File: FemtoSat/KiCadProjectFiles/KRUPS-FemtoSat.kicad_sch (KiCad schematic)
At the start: 51 parts, among them J1 XT30U Male Connector, J2 54-00170, J3 USB_C_Receptacle_USB2.0_16P, Q1 IRF7410, Q2 IRF7410, SW1 Enable Switch, SW2 Enclosure Detector, SW3 Enclosure Detector, U1 BME280, U2 ESP32-S3-WROOM-2, U3 TSR_2-2450, U4 TPS61023, U5 E22-900M33S, U6 TPS2117, U7 BNO086, U8 AZ1117-3.3

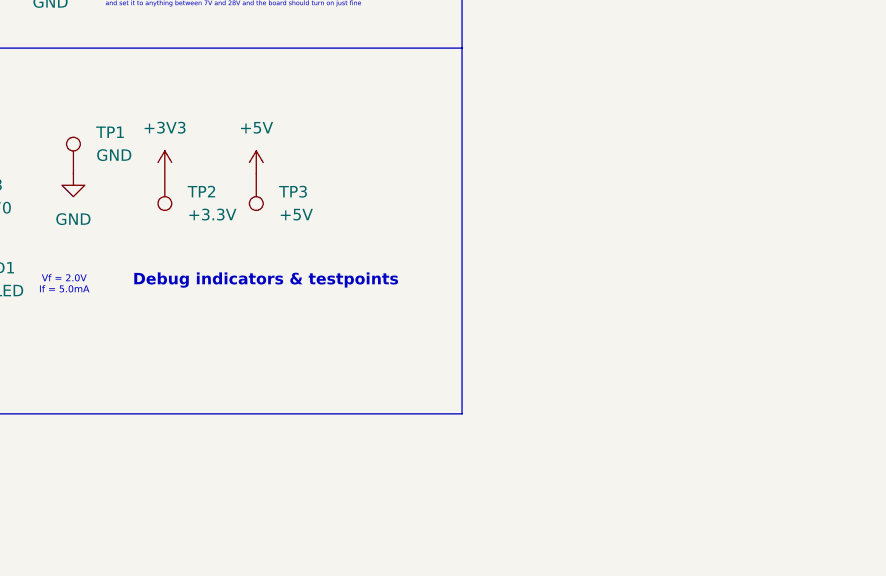
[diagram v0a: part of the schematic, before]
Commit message: Added optional support for the LR62XE 1W radio
- Created a breakout/adapter board for the LR62XE 1W LoRa radio
- Modified the FemtoSat and RocketStation so that they'll be compatible with the adapter board
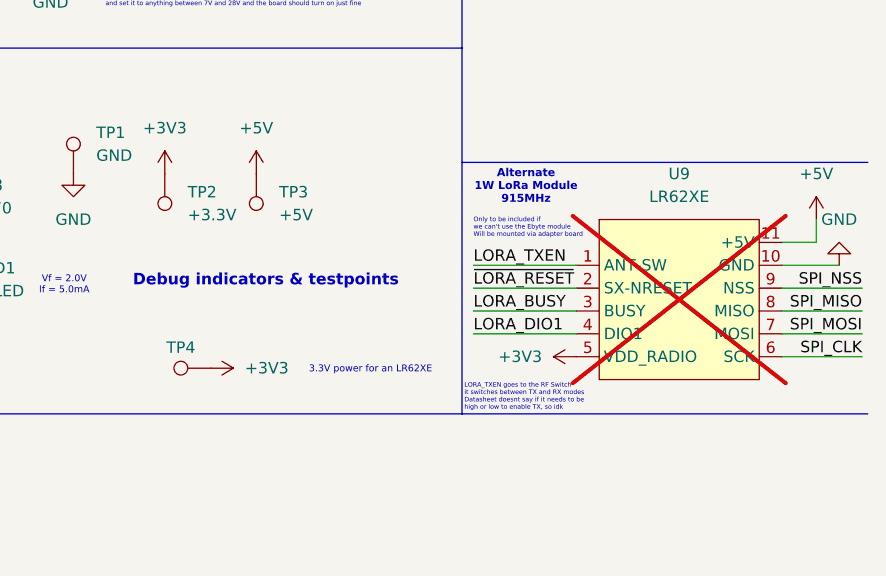
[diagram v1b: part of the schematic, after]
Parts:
- added TP4: TestPoint, TestPoint:TestPoint_Pad_2.0x2.0mm, symbol Connector:TestPoint
- added U9: LR62XE, KRUPS-FemtoSat:LR62XE, symbol KRUPS-FemtoSat:LR62XE
- U5: now left out of the parts list
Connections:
- net +3V3: now also TP4.1, U9.5 (VDD_RADIO)
- net +5V: now also U9.11 (+5V)
- net GND: now also U9.10 (GND), U9.12 (GND)
- net LORA_BUSY: now also U9.3 (BUSY)
- net LORA_DIO1: now also U9.4 (DIO1)
- net LORA_TXEN: now also U9.1 (ANT-SW)
- net SPI_CLK: now also U9.6 (SCK)
- net SPI_MISO: now also U9.8 (MISO)
- net SPI_MOSI: now also U9.7 (MOSI)
- net SPI_NSS: now also U9.9 (NSS)
- net ~{LORA_RESET}: now also U9.2 (SX-NRESET)
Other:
- note added: "3.3V power for an LR62XE"
- note added: "Alternate 1W LoRa Module 915MHz"
- note added: "LORA_TXEN goes to the RF Switch it switches between TX and RX modes Datasheet doesnt say if it needs to be high or low to enable TX, so idk"
- note added: "Only to be included if we can't use the Ebyte module Will be mounted via adapter board"

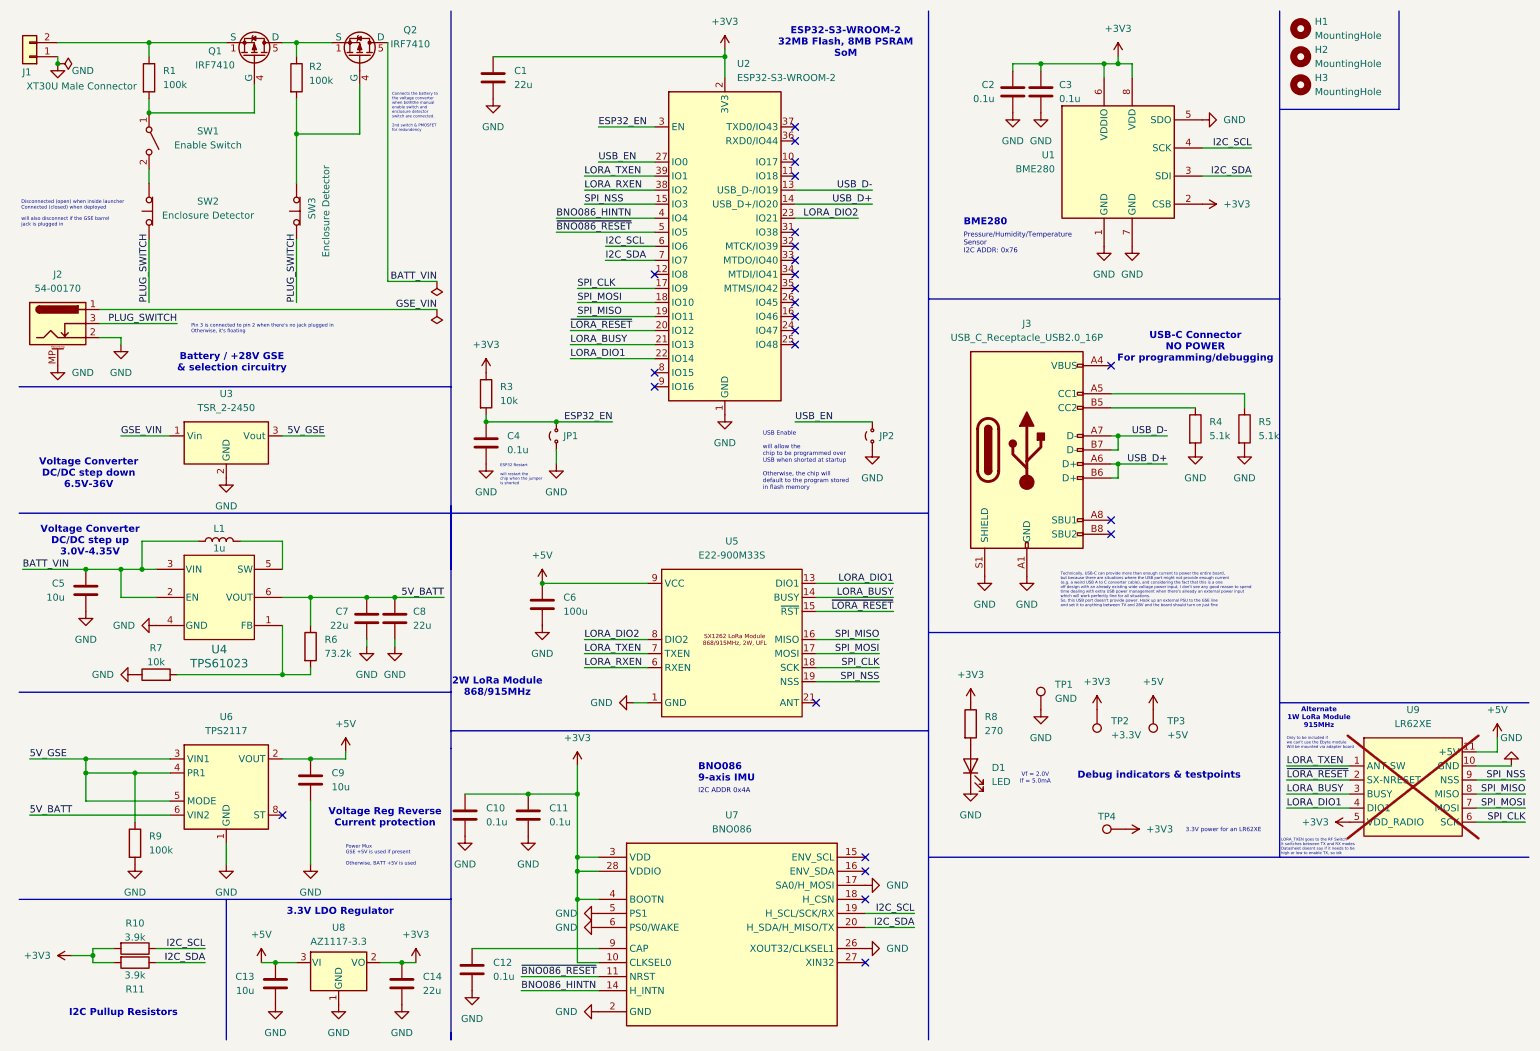
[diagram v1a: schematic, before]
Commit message: Design Review Updates
Large number of design changes to both the FemtoSat (V5) and RocketStation (V3)

On both boards:
- Swapped the ESP32-S3-WROOM-2 modules to WROOM-1 modules due to supply issues
- Swapped power connectors to JST VH, data connectors to JST GH
- Added "Space Systems Lab, University of Kentucky, Lexington KY, USA, Earth" to the silkscreens
- Added test pads for IO pins, I2C bus, power
- Added LEDs connected to IO pins
- Changed power indication LEDs to a brighter LED
- Reformatted BOMs, they can now be generated by KiCad rather than being made by hand
- Updated documentation, 3D models

For Femtosat
- Removed 1 enclosure switch & MOSFET
- Moved a screw hole

and a bunch of other minor changes that I've forgotten
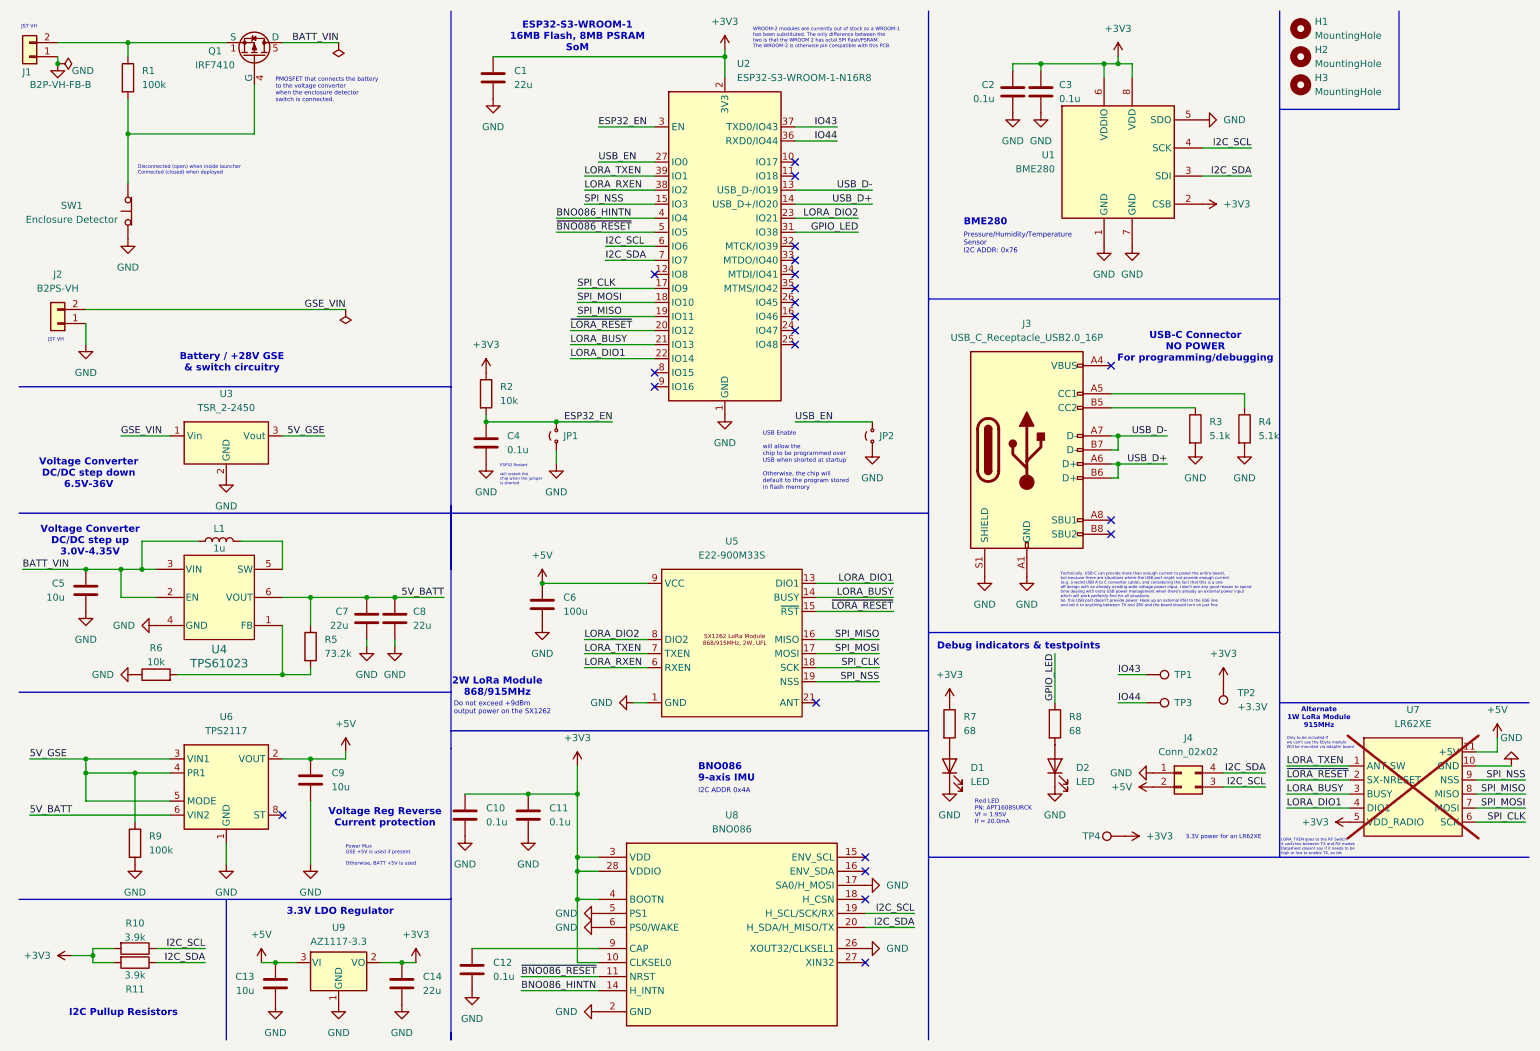
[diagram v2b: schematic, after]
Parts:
- removed J2: 54-00170, KRUPS-FemtoSat:TENSILITY_54-00170, symbol Connector:Barrel_Jack_Switch_MountingPin
- removed Q2: IRF7410, Package_SO:SOIC-8_3.9x4.9mm_P1.27mm, symbol KRUPS-FemtoSat:IRF7410
- removed R2: 100k, Resistor_SMD:R_0603_1608Metric_Pad0.98x0.95mm_HandSolder, symbol Device:R
- removed SW1: Enable Switch, Button_Switch_THT:SW_DIP_SPSTx01_Slide_6.7x4.1mm_W7.62mm_P2.54mm_LowProfile, symbol Switch:SW_SPST
- removed SW3: Enclosure Detector, KRUPS-FemtoSat:LC1258OANP, symbol Switch:SW_Push_Open
- added D2: LED, Diode_SMD:D_0603_1608Metric_Pad1.05x0.95mm_HandSolder, symbol Device:LED
- added J2: B2PS-VH, Connector_JST:JST_VH_S2P-VH_1x02_P3.96mm_Horizontal, symbol Connector_Generic:Conn_01x02
- added J4: Conn_02x02, Connector_PinHeader_2.54mm:PinHeader_2x02_P2.54mm_Vertical, symbol Connector_Generic:Conn_02x02_Counter_Clockwise
- added R8: 68, Resistor_SMD:R_0603_1608Metric_Pad0.98x0.95mm_HandSolder, symbol Device:R
- C1, C14, C7, C8: Digikey Part Number (none) -> CL21A226MPQNNNE
- C10, C11, C12, C2, C3, C4: Digikey Part Number (none) -> CC0603KRX7R7BB104
- C13, C5, C9: Digikey Part Number (none) -> CL21A106KOQNNNG
- C6: Digikey Part Number (none) -> CL31A107MQHNNWE
- D1: Digikey Part Number (none) -> APT1608SURCK
- J1: value XT30U Male Connector -> B2P-VH-FB-B; footprint Connector_AMASS:AMASS_XT30U-M_1x02_P5.0mm_Vertical -> Connector_JST:JST_VH_B2P-VH-FB-B_1x02_P3.96mm_Vertical; Digikey Part Number (none) -> B2P-VH-FB-B
- J3: Digikey Part Number (none) -> USB4110-GF-A
- L1: Digikey Part Number (none) -> XEL4030-102MEC
- Q1: Digikey Part Number (none) -> IRF7410TRPBF
- R1, R9: Digikey Part Number (none) -> RMCF0603FT100K
- R10, R11: Digikey Part Number (none) -> ERJ-3EKF3901V
- R2: renamed from R3; Digikey Part Number (none) -> RC0603FR-0710KL
- R3: renamed from R4; Digikey Part Number (none) -> RC0603FR-075K1L
- R4: renamed from R5; Digikey Part Number (none) -> RC0603FR-075K1L
- R5: renamed from R6; Digikey Part Number (none) -> RC0603FR-0773K2L
- R6: renamed from R7; Digikey Part Number (none) -> RC0603FR-0710KL
- R7: renamed from R8; value 270 -> 68; Digikey Part Number (none) -> RC0603JR-0768RL
- SW1: renamed from SW2; Digikey Part Number (none) -> LC1258OANP
- TP1: value GND -> TestPoint; footprint TestPoint:TestPoint_Pad_1.5x1.5mm -> TestPoint:TestPoint_Pad_D2.0mm
- TP3: value +5V -> TestPoint; footprint TestPoint:TestPoint_Pad_1.5x1.5mm -> TestPoint:TestPoint_Pad_D2.0mm
- U1: Digikey Part Number (none) -> BME280
- U2: value ESP32-S3-WROOM-2 -> ESP32-S3-WROOM-1-N16R8; Digikey Part Number (none) -> ESP32-S3-WROOM-1-N16R8
- U3: Digikey Part Number (none) -> TSR 2-2450
- U4: Digikey Part Number (none) -> TPS61023DRLR
- U5: Digikey Part Number (none) -> ORDER SEPERATELY
- U6: Digikey Part Number (none) -> TPS2117DRLR
- U7: renamed from U9; Digikey Part Number (none) -> LR62XE
- U8: renamed from U7; Digikey Part Number (none) -> BNO086
- U9: renamed from U8; Digikey Part Number (none) -> AZ1117CR2-3.3TRG1
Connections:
- net PLUG_SWITCH is gone; now on net GND: SW1.1 (A)
- net +5V: now also J4.2 (Pin_2); no longer TP3.1
- net BATT_VIN: now also Q1.5 (D), Q1.6, Q1.7, Q1.8
- net GND: now also D2.1 (K), J2.1 (Pin_1), J4.1 (Pin_1); no longer TP1.1
- net GSE_VIN: now also J2.2 (Pin_2)
- net I2C_SCL: now also J4.3 (Pin_3)
- net I2C_SDA: now also J4.4 (Pin_4)
- net at Q1.4 (G), R1.2: now also SW1.2 (B)
- net GPIO_LED: now reaches U2.31 (IO38)
- net GPIO_LED: now also R8.1
- net IO44: now reaches U2.36 (RXD0/IO44)
- net IO44: now also TP3.1
- net IO43: now reaches U2.37 (TXD0/IO43)
- net IO43: now also TP1.1
- new net: D2.2 (A), R8.2
- no-connect marks 25 -> 22
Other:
- note added: "Battery / +28V GSE & switch circuitry"
- note added: "Disconnected (open) when inside launcher Connected (closed) when deployed"
- note added: "Do not exceed +9dBm output power on the SX1262"
- note added: "ESP32-S3-WROOM-1 16MB Flash, 8MB PSRAM SoM"
- note added: "JST VH"
- note added: "PMOSFET that connects the battery to the voltage converter when the enclosure detector switch is connected."
- note added: "Red LED PN: APT1608SURCK Vf = 1.95V If = 20.0mA"
- note added: "WROOM-2 modules are currently out of stock so a WROOM-1 has been substituted. The only difference between the two is that the WROOM 2 has octal SPI flash/PSRAM. The WROOM-2 is otherwise pin compatible with this PCB."
- note removed: "Battery / +28V GSE & selection circuitry"
- note removed: "Connects the battery to the voltage converter when boththe manual enable switch and enclosure detector switch are connected. 2nd switch & PMOSFET for redundency"
- note removed: "Disconnected (open) when inside launcher Connected (closed) when deployed will also disconnect if the GSE barrel jack is plugged in"
- note removed: "ESP32-S3-WROOM-2 32MB Flash, 8MB PSRAM SoM"
- note removed: "Pin 3 is connected to pin 2 when there's no jack plugged in Otherwise, it's floating"
- note removed: "Vf = 2.0V If = 5.0mA"
- moved on the sheet: D1, R1, R7, SW1, TP2, TP4

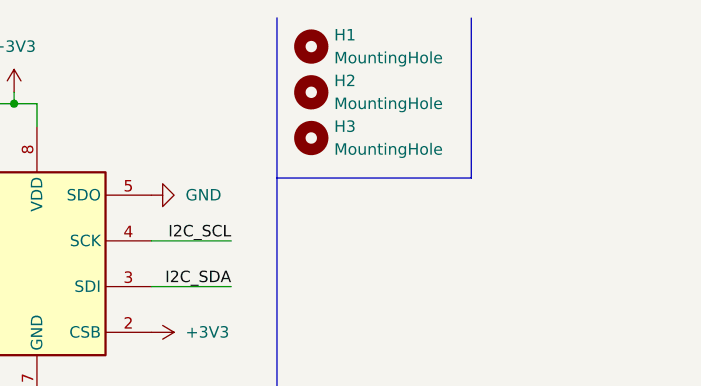
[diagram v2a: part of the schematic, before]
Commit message: Added fiducials to femtosat (v6) and rocketstation (v4)
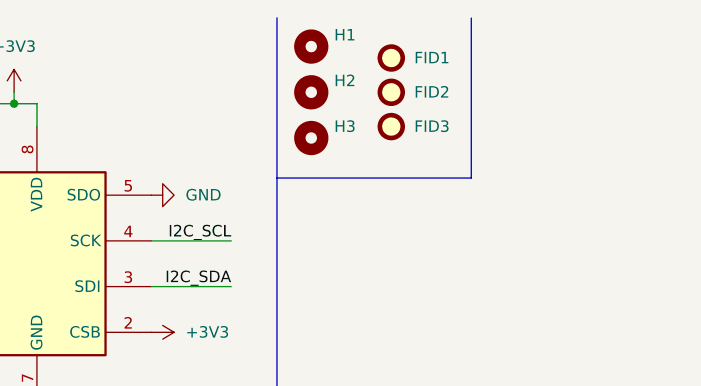
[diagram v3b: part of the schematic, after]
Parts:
- added FID1, FID2, FID3: Fiducial, Fiducial:Fiducial_0.5mm_Mask1mm, symbol Mechanical:Fiducial
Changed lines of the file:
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@@
 	(paper "A4")
 	(title_block
-		(date "2024-12-27")
-		(rev "V5")
+		(date "2024-12-28")
+		(rev "V6")
 	)
 	(junction
@@
 				)
 				(justify left)
+				(hide yes)
 			)
 		)
@@
 				)
 				(justify left)
+				(hide yes)
 			)
 		)
@@
 				)
 				(justify left)
+				(hide yes)
 			)
 		)
@@
 	)
 	(symbol
+		(lib_id "Mechanical:Fiducial")
+		(at 252.73 16.51 0)
+		(unit 1)
+		(exclude_from_sim yes)
+		(in_bom no)
+		(on_board yes)
+		(dnp no)
+		(property "Reference" "FID1"
+			(at 255.27 16.51 0)
+			(effects
+				(font
+					(size 1.27 1.27)
+				)
+				(justify left)
+			)
+		)
+		(property "Value" "Fiducial"
+			(at 255.27 17.7799 0)
+			(effects
+				(font
+					(size 1.27 1.27)
+				)
+				(justify left)
+				(hide yes)
+			)
+		)
+		(property "Footprint" "Fiducial:Fiducial_0.5mm_Mask1mm"
+			(at 252.73 16.51 0)
+			(effects
+				(font
+					(size 1.27 1.27)
+				)
+				(hide yes)
+			)
+		)
+		(property "Datasheet" "~"
+			(at 252.73 16.51 0)
+			(effects
+				(font
+					(size 1.27 1.27)
+				)
+				(hide yes)
+			)
+		)
+		(property "Description" "Fiducial Marker"
+			(at 252.73 16.51 0)
+			(effects
+				(font
+					(size 1.27 1.27)
+				)
+				(hide yes)
+			)
+		)
+		(instances
+			(project ""
+				(path "/b0dcfc14-9606-45df-8d55-b7b091984c61"
+					(reference "FID1")
+					(unit 1)
+				)
+			)
+		)
+	)
+	(symbol
 		(lib_id "power:PWR_FLAG")
 		(at 19.05 21.59 270)
@@
 	)
 	(symbol
+		(lib_id "Mechanical:Fiducial")
+		(at 252.73 20.32 0)
+		(unit 1)
+		(exclude_from_sim yes)
+		(in_bom no)
+		(on_board yes)
+		(dnp no)
+		(property "Reference" "FID2"
+			(at 255.27 20.32 0)
+			(effects
+				(font
+					(size 1.27 1.27)
+				)
+				(justify left)
+			)
+		)
+		(property "Value" "Fiducial"
+			(at 255.27 21.5899 0)
+			(effects
+				(font
+					(size 1.27 1.27)
+				)
+				(justify left)
+				(hide yes)
+			)
+		)
+		(property "Footprint" "Fiducial:Fiducial_0.5mm_Mask1mm"
+			(at 252.73 20.32 0)
+			(effects
+				(font
+					(size 1.27 1.27)
+				)
+				(hide yes)
+			)
+		)
+		(property "Datasheet" "~"
+			(at 252.73 20.32 0)
+			(effects
+				(font
+					(size 1.27 1.27)
+				)
+				(hide yes)
+			)
+		)
+		(property "Description" "Fiducial Marker"
+			(at 252.73 20.32 0)
+			(effects
+				(font
+					(size 1.27 1.27)
+				)
+				(hide yes)
+			)
+		)
+		(instances
+			(project "KRUPS-FemtoSat"
+				(path "/b0dcfc14-9606-45df-8d55-b7b091984c61"
+					(reference "FID2")
+					(unit 1)
+				)
+			)
+		)
+	)
+	(symbol
 		(lib_id "power:GND")
 		(at 116.84 177.8 270)
@@
 					(unit 1)
 				)
+			)
+		)
+	)
+	(symbol
+		(lib_id "Mechanical:Fiducial")
+		(at 252.73 24.13 0)
+		(unit 1)
+		(exclude_from_sim yes)
+		(in_bom no)
+		(on_board yes)
+		(dnp no)
+		(property "Reference" "FID3"
+			(at 255.27 24.13 0)
+			(effects
+				(font
+					(size 1.27 1.27)
+				)
+				(justify left)
+			)
+		)
+		(property "Value" "Fiducial"
+			(at 255.27 25.3999 0)
+			(effects
+				(font
+					(size 1.27 1.27)
+				)
+				(justify left)
+				(hide yes)
+			)
+		)
+		(property "Footprint" "Fiducial:Fiducial_0.5mm_Mask1mm"
+			(at 252.73 24.13 0)
+			(effects
+				(font
+					(size 1.27 1.27)
+				)
+				(hide yes)
+			)
+		)
+		(property "Datasheet" "~"
+			(at 252.73 24.13 0)
+			(effects
+				(font
+					(size 1.27 1.27)
+				)
+				(hide yes)
+			)
+		)
+		(property "Description" "Fiducial Marker"
+			(at 252.73 24.13 0)
+			(effects
+				(font
+					(size 1.27 1.27)
+				)
+				(hide yes)
+			)
+		)
+		(instances
+			(project "KRUPS-FemtoSat"
+				(path "/b0dcfc14-9606-45df-8d55-b7b091984c61"
+					(reference "FID3")
+					(unit 1)
+				)
